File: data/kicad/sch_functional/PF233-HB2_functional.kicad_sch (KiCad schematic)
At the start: 10 parts

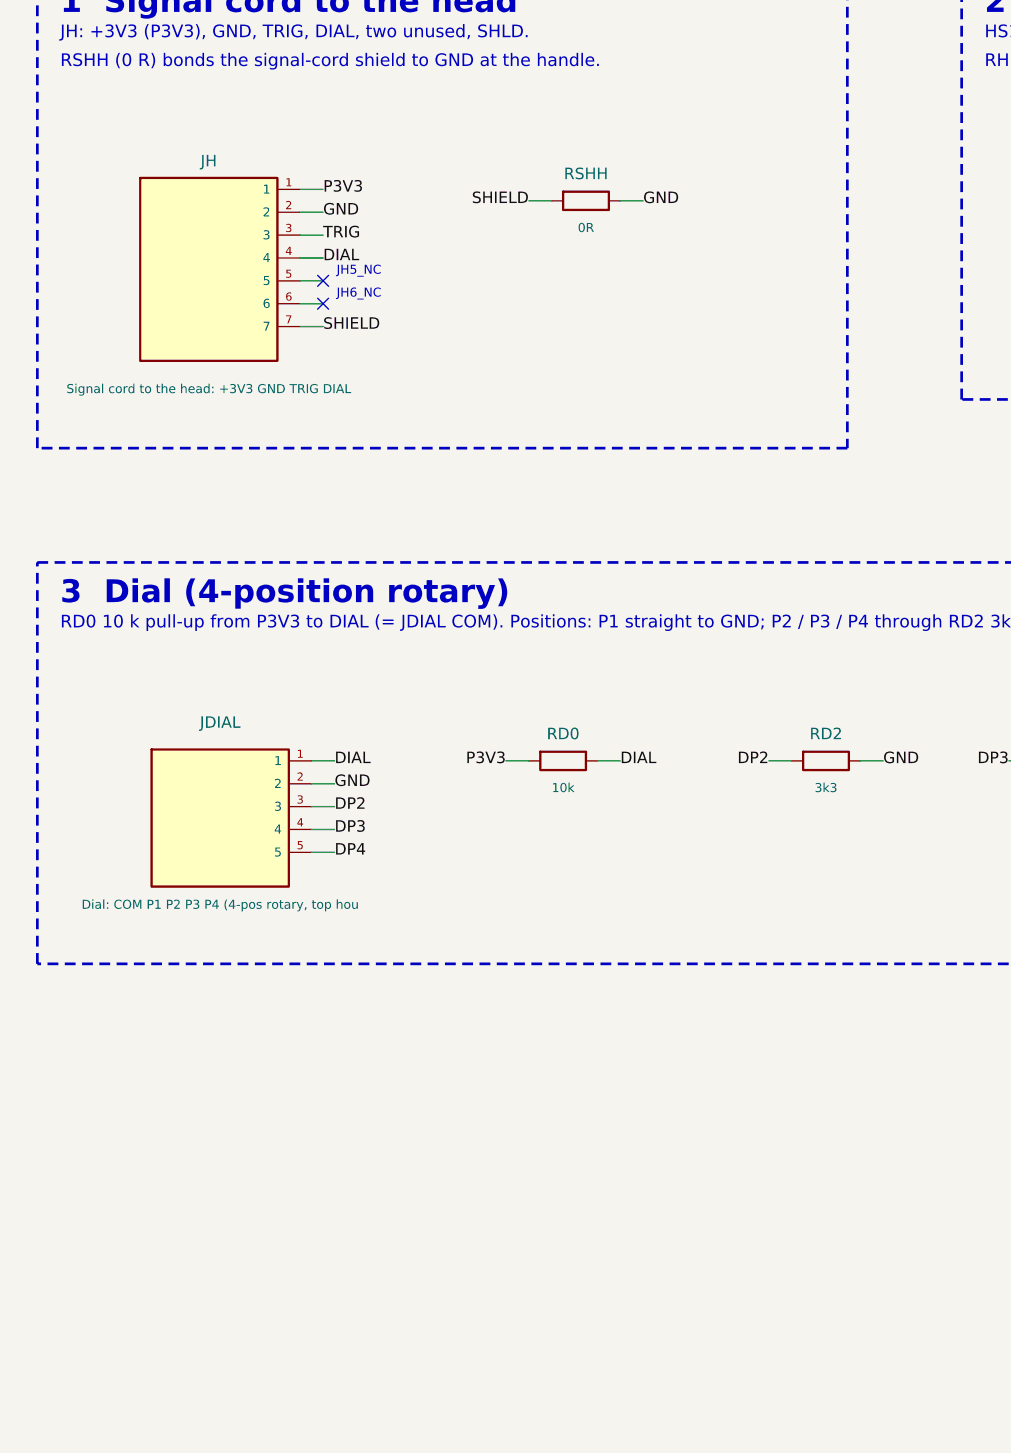
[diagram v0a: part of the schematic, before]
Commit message: WIP (NOT signed off): data published by the first close-out sign-off run, which had 5 FAIL (CB1D-C2 / AU1 fine-pitch clearance); superseded by the rerun in progress
Co-Authored-By: Claude Opus 5.5 <noreply@anthropic.com>
Claude-Session: https://claude.ai/code/session_01FX4DWSYYjMCFGGA6gmha65
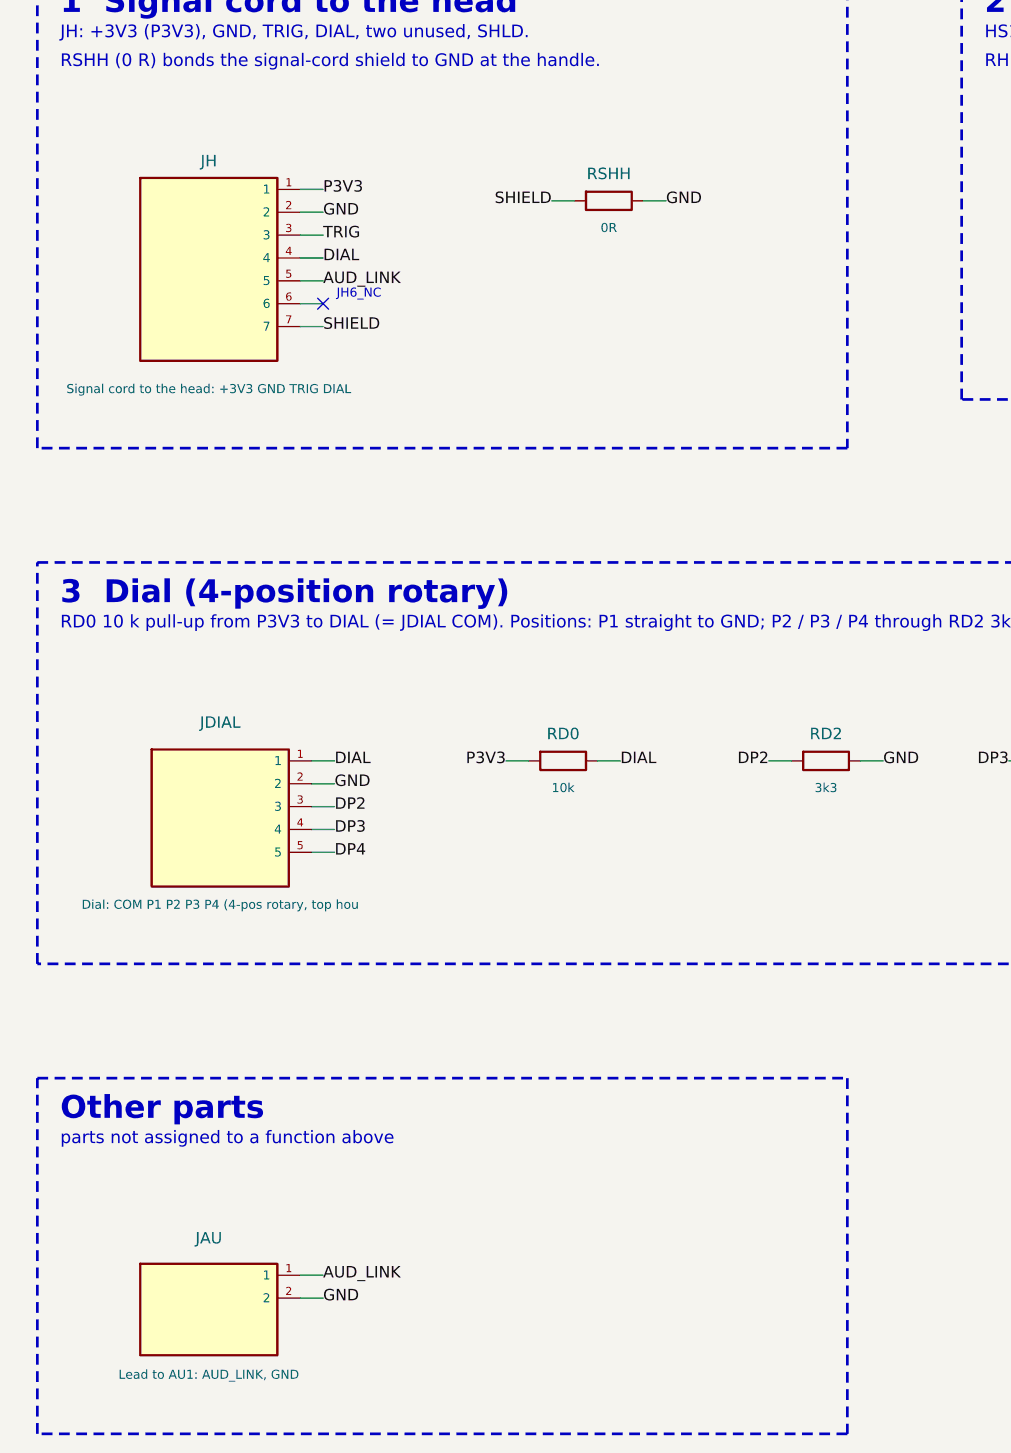
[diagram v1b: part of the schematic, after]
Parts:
- added JAU: Lead to AU1: AUD_LINK, GND, Connector:SolderPad_2x_P5.08mm, symbol PF233F:BOX_WIRE2
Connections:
- net GND: now also JAU.2
- net AUD_LINK: now reaches JH.5
- net AUD_LINK: now also JAU.1
- no-connect marks 2 -> 1
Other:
- note added: "Other parts"
- note added: "parts not assigned to a function above"
- note removed: "JH5_NC"
- moved on the sheet: RSHH
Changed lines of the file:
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@@
-(kicad_sch (version 20231120) (generator "arx_sch_func") (generator_version "1") (paper "User" 304.8 203.2)
+(kicad_sch (version 20231120) (generator "arx_sch_func") (generator_version "1") (paper "User" 304.8 254.0)
   (title_block (title "PF233-HB2  functional schematic") (date "2026-10-26") (rev "r3") (company "ARX / PHI-FOLD 233") (comment 1 "HB2 grip board: Hall trigger, 4-position dial divider, signal cord") (comment 2 "MODELED design: not built, not bench-tested.") (comment 3 "Generated: src/pcb/sch_func.py; checked against the netlist."))
   (text "How to read: parts sit in functional blocks (dashed frames). Every pin ends in a short wire with its NET NAME; equal names are connected (also between blocks). A cross = intentionally unconnected pin." (exclude_from_sim no) (at 20.320 10.160 0) (effects (font (size 1.4 1.4)) (justify left top)))
@@
   (label "DIAL" (at 52.070 69.850 0) (fields_autoplaced yes) (effects (font (size 1.27 1.27)) (justify left)))
   (wire (pts (xy 49.530 72.390) (xy 52.070 72.390)) (stroke (width 0) (type default)))
-  (no_connect (at 52.070 72.390))
-  (text "JH5_NC" (exclude_from_sim no) (at 53.570 71.390 0) (effects (font (size 1.0 1.0)) (justify left)))
+  (label "AUD_LINK" (at 52.070 72.390 0) (fields_autoplaced yes) (effects (font (size 1.27 1.27)) (justify left)))
   (wire (pts (xy 49.530 74.930) (xy 52.070 74.930)) (stroke (width 0) (type default)))
   (no_connect (at 52.070 74.930))
@@
   (wire (pts (xy 49.530 77.470) (xy 52.070 77.470)) (stroke (width 0) (type default)))
   (label "SHIELD" (at 52.070 77.470 0) (fields_autoplaced yes) (effects (font (size 1.27 1.27)) (justify left)))
-  (symbol (lib_id "PF233F:R_H") (at 81.280 63.500 0) (unit 1) (exclude_from_sim no) (in_bom yes) (on_board yes) (dnp no)
-    (property "Reference" "RSHH" (at 81.280 60.500 0) (effects (font (size 1.27 1.27))))
-    (property "Value" "0R" (at 81.280 66.500 0) (effects (font (size 1.0 1.0))))
-    (property "Footprint" "Resistor_SMD:R_0603_1608Metric" (at 81.280 63.500 0) (effects (font (size 1.27 1.27)) hide))
+  (symbol (lib_id "PF233F:R_H") (at 83.820 63.500 0) (unit 1) (exclude_from_sim no) (in_bom yes) (on_board yes) (dnp no)
+    (property "Reference" "RSHH" (at 83.820 60.500 0) (effects (font (size 1.27 1.27))))
+    (property "Value" "0R" (at 83.820 66.500 0) (effects (font (size 1.0 1.0))))
+    (property "Footprint" "Resistor_SMD:R_0603_1608Metric" (at 83.820 63.500 0) (effects (font (size 1.27 1.27)) hide))
     (pin "1")
     (pin "2")
     (instances (project "PF233-HB2" (path "/bb4a35e1-3309-5233-ab71-8e6b47a7fd86" (reference "RSHH") (unit 1))))
   )
-  (wire (pts (xy 77.470 63.500) (xy 74.930 63.500)) (stroke (width 0) (type default)))
-  (label "SHIELD" (at 74.930 63.500 180) (fields_autoplaced yes) (effects (font (size 1.27 1.27)) (justify right)))
-  (wire (pts (xy 85.090 63.500) (xy 87.630 63.500)) (stroke (width 0) (type default)))
-  (label "GND" (at 87.630 63.500 0) (fields_autoplaced yes) (effects (font (size 1.27 1.27)) (justify left)))
+  (wire (pts (xy 80.010 63.500) (xy 77.470 63.500)) (stroke (width 0) (type default)))
+  (label "SHIELD" (at 77.470 63.500 180) (fields_autoplaced yes) (effects (font (size 1.27 1.27)) (justify right)))
+  (wire (pts (xy 87.630 63.500) (xy 90.170 63.500)) (stroke (width 0) (type default)))
+  (label "GND" (at 90.170 63.500 0) (fields_autoplaced yes) (effects (font (size 1.27 1.27)) (justify left)))
   (rectangle (start 123.02 38.10) (end 241.43 85.57) (stroke (width 0.3) (type dash)) (fill (type none)))
   (text "2  Hall trigger" (exclude_from_sim no) (at 125.560 40.100 0) (effects (font (size 2.54 2.54) bold) (justify left top)))
@@
   (wire (pts (xy 166.370 125.730) (xy 168.910 125.730)) (stroke (width 0) (type default)))
   (label "GND" (at 168.910 125.730 0) (fields_autoplaced yes) (effects (font (size 1.27 1.27)) (justify left)))
+  (rectangle (start 20.32 160.98) (end 110.32 200.50) (stroke (width 0.3) (type dash)) (fill (type none)))
+  (text "Other parts" (exclude_from_sim no) (at 22.860 162.980 0) (effects (font (size 2.54 2.54) bold) (justify left top)))
+  (text "parts not assigned to a function above" (exclude_from_sim no) (at 22.860 166.980 0) (effects (font (size 1.4 1.4)) (justify left top)))
+  (symbol (lib_id "PF233F:BOX_WIRE2") (at 39.370 186.690 0) (unit 1) (exclude_from_sim no) (in_bom yes) (on_board yes) (dnp no)
+    (property "Reference" "JAU" (at 39.370 178.760 0) (effects (font (size 1.27 1.27))))
+    (property "Value" "Lead to AU1: AUD_LINK, GND" (at 39.370 193.920 0) (effects (font (size 1.0 1.0))))
+    (property "Footprint" "Connector:SolderPad_2x_P5.08mm" (at 39.370 186.690 0) (effects (font (size 1.27 1.27)) hide))
+    (pin "1")
+    (pin "2")
+    (instances (project "PF233-HB2" (path "/bb4a35e1-3309-5233-ab71-8e6b47a7fd86" (reference "JAU") (unit 1))))
+  )
+  (wire (pts (xy 49.530 182.880) (xy 52.070 182.880)) (stroke (width 0) (type default)))
+  (label "AUD_LINK" (at 52.070 182.880 0) (fields_autoplaced yes) (effects (font (size 1.27 1.27)) (justify left)))
+  (wire (pts (xy 49.530 185.420) (xy 52.070 185.420)) (stroke (width 0) (type default)))
+  (label "GND" (at 52.070 185.420 0) (fields_autoplaced yes) (effects (font (size 1.27 1.27)) (justify left)))
   (sheet_instances (path "/" (page "1")))
 )

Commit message: WIP (NOT signed off): data published by the second close-out run (8 FAIL: 3 opens on CB1D-C2 / AU1 under the exact fine-zone keep-out); third run in progress
Co-Authored-By: Claude Opus 5.5 <noreply@anthropic.com>
Claude-Session: https://claude.ai/code/session_01FX4DWSYYjMCFGGA6gmha65
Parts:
- JDIAL: symbol PF233F:BOX_HDR1x5 -> PF233F:BOX_WIRE1x5
- JH: symbol PF233F:BOX_HDR1x7 -> PF233F:BOX_WIRE1x7
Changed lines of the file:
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@@
   (text "JH: +3V3 (P3V3), GND, TRIG, DIAL, two unused, SHLD." (exclude_from_sim no) (at 22.860 44.100 0) (effects (font (size 1.4 1.4)) (justify left top)))
   (text "RSHH (0 R) bonds the signal-cord shield to GND at the handle." (exclude_from_sim no) (at 22.860 47.300 0) (effects (font (size 1.4 1.4)) (justify left top)))
-  (symbol (lib_id "PF233F:BOX_HDR1x7") (at 39.370 71.120 0) (unit 1) (exclude_from_sim no) (in_bom yes) (on_board yes) (dnp no)
+  (symbol (lib_id "PF233F:BOX_WIRE1x7") (at 39.370 71.120 0) (unit 1) (exclude_from_sim no) (in_bom yes) (on_board yes) (dnp no)
     (property "Reference" "JH" (at 39.370 59.080 0) (effects (font (size 1.27 1.27))))
     (property "Value" "Signal cord to the head: +3V3 GND TRIG DIAL " (at 39.370 84.400 0) (effects (font (size 1.0 1.0))))
@@
   (text "3  Dial (4-position rotary)" (exclude_from_sim no) (at 22.860 105.680 0) (effects (font (size 2.54 2.54) bold) (justify left top)))
   (text "RD0 10 k pull-up from P3V3 to DIAL (= JDIAL COM). Positions: P1 straight to GND; P2 / P3 / P4 through RD2 3k3 / RD3 10 k / RD4 33 k to GND, so each position gives a different divider level." (exclude_from_sim no) (at 22.860 109.680 0) (effects (font (size 1.4 1.4)) (justify left top)))
-  (symbol (lib_id "PF233F:BOX_HDR1x5") (at 40.640 132.080 0) (unit 1) (exclude_from_sim no) (in_bom yes) (on_board yes) (dnp no)
+  (symbol (lib_id "PF233F:BOX_WIRE1x5") (at 40.640 132.080 0) (unit 1) (exclude_from_sim no) (in_bom yes) (on_board yes) (dnp no)
     (property "Reference" "JDIAL" (at 40.640 121.460 0) (effects (font (size 1.27 1.27))))
     (property "Value" "Dial: COM P1 P2 P3 P4 (4-pos rotary, top hou" (at 40.640 141.700 0) (effects (font (size 1.0 1.0))))

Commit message: Close-out of the output modes / audio / gyro integration: sign-off 76 PASS / 0 FAIL / 4 UNVERIFIED, strict regress 114 / 0, release controls 12 / 12, publish 0 stale
AU1 (36 x 60, 8 layers, gyro moved from CB1D) routed 38 / 38, CB1D-C2 46 / 46, both exact DRC 0 / 0; PB1R-v5 AWG12 solder holes; PM2-B, HB2-B; superseded Gerber sets marked.
Tooling now default: exact-geometry DRC, router fine-pitch keep-out / neck-down / per-board grid, local repair, round checkpoints, non-destructive reset,
interface check, AU1 3-D models with gull-wing leads, counted HV check; pad check traced by the pipeline; process-guard regress row; PROCESS.md / CLAUDE.md / handoff updated.

Co-Authored-By: Claude Opus 5.5 <noreply@anthropic.com>
Claude-Session: https://claude.ai/code/session_01FX4DWSYYjMCFGGA6gmha65
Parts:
- JDIAL: footprint Connector:Pin_header_1x5_P2.54mm -> Connector:Wire_pads_1x5_P2.54mm
- JH: footprint Connector:Pin_header_1x7_P2.54mm -> Connector:Wire_pads_1x7_P2.54mm
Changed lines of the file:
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@@
     (property "Reference" "JH" (at 39.370 59.080 0) (effects (font (size 1.27 1.27))))
     (property "Value" "Signal cord to the head: +3V3 GND TRIG DIAL " (at 39.370 84.400 0) (effects (font (size 1.0 1.0))))
-    (property "Footprint" "Connector:Pin_header_1x7_P2.54mm" (at 39.370 71.120 0) (effects (font (size 1.27 1.27)) hide))
+    (property "Footprint" "Connector:Wire_pads_1x7_P2.54mm" (at 39.370 71.120 0) (effects (font (size 1.27 1.27)) hide))
     (pin "1")
     (pin "2")
@@
     (property "Reference" "JDIAL" (at 40.640 121.460 0) (effects (font (size 1.27 1.27))))
     (property "Value" "Dial: COM P1 P2 P3 P4 (4-pos rotary, top hou" (at 40.640 141.700 0) (effects (font (size 1.0 1.0))))
-    (property "Footprint" "Connector:Pin_header_1x5_P2.54mm" (at 40.640 132.080 0) (effects (font (size 1.27 1.27)) hide))
+    (property "Footprint" "Connector:Wire_pads_1x5_P2.54mm" (at 40.640 132.080 0) (effects (font (size 1.27 1.27)) hide))
     (pin "1")
     (pin "2")
